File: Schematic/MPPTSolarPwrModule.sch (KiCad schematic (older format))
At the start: 87 parts, among them J1 Screw_Terminal_01x02, J10 Conn_01x02, J11 Conn_01x02, J2 Conn_01x02, J3 Conn_01x03, J4 Conn_01x02, J5 Conn_01x02, J6 Conn_01x03, J7 Conn_01x04, J8 Conn_01x06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

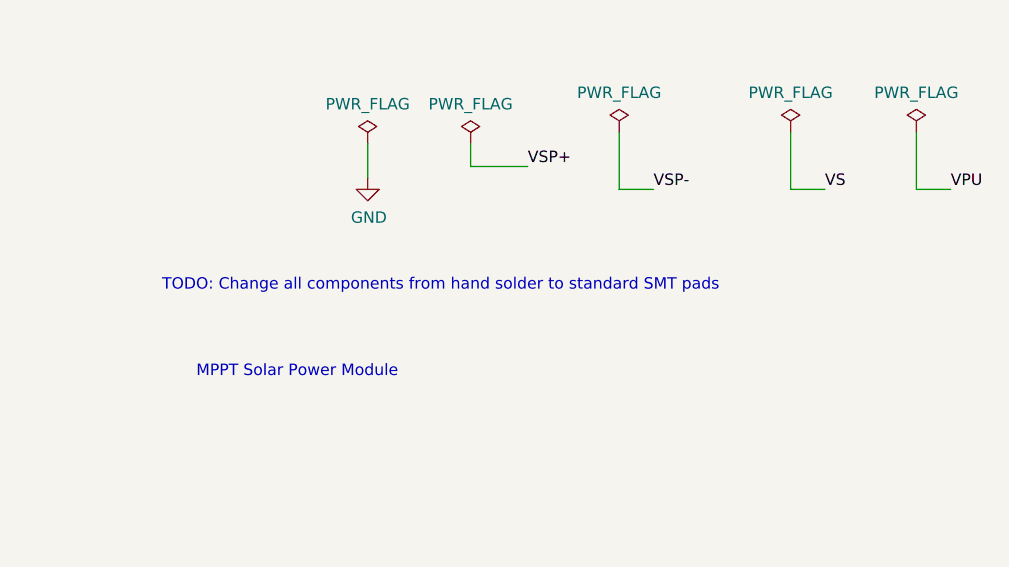
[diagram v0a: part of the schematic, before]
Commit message: Added KiCad 3D models, Documents, and updated schematic
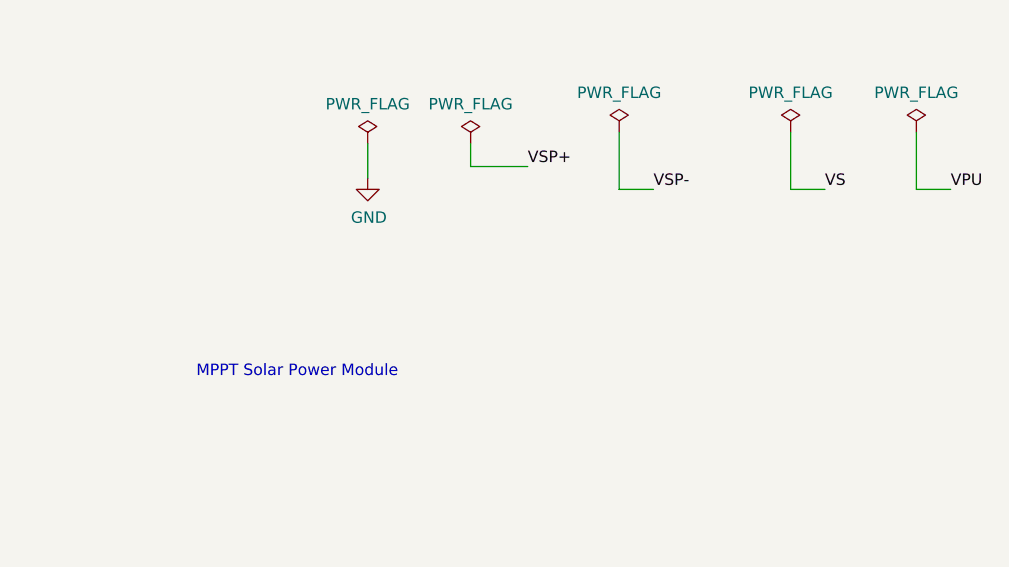
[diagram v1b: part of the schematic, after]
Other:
- note removed: "TODO: Change all components from hand solder to standard SMT pads"
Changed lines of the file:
@@
 Wire Wire Line
 	8950 7450 10300 7450
-Text Notes 12650 9150 0    50   ~ 0
-TODO: Change all components from hand solder to standard SMT pads
 $Comp
 L Connector_Generic:Conn_01x02 J11
